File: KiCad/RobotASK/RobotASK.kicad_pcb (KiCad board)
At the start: 2 copper layers, 80 x 50 mm, 14 parts, among them J1 Conn_01x04_Pin, J2 Conn_01x04_Pin, J3 Conn_01x04_Pin, J4 Conn_01x04_Pin, J5 Conn_01x04_Pin, J6 Conn_01x04_Pin, J7 Conn_01x02_Pin, J8 Conn_01x03_Pin, SW2 SW_Omron_B3FS, U1 ATmega328-P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

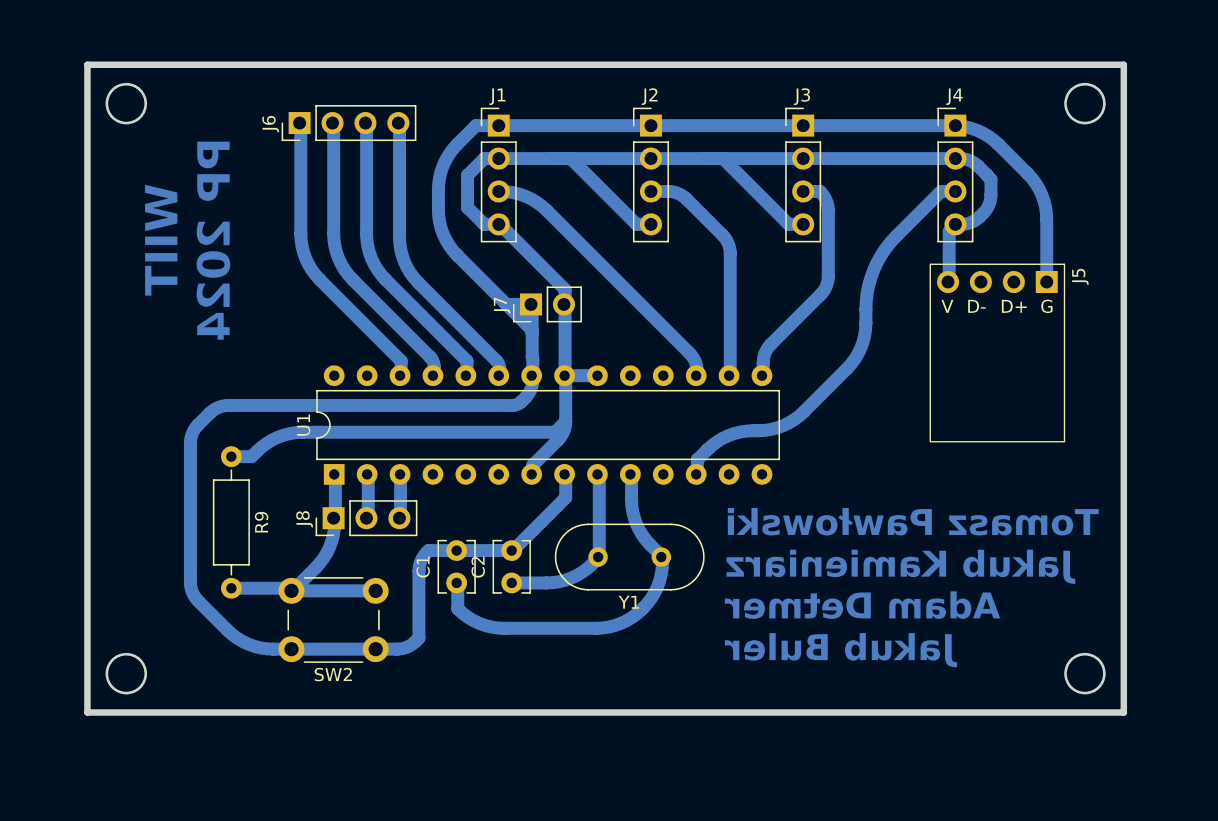
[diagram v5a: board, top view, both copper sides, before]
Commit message: Poprawki kodu, zwiększenie otworów na komponenty na 1mm, nowe wydruki do termotransferu i nawiercania otworów, poukładanie nieaktualnych wydruków UV
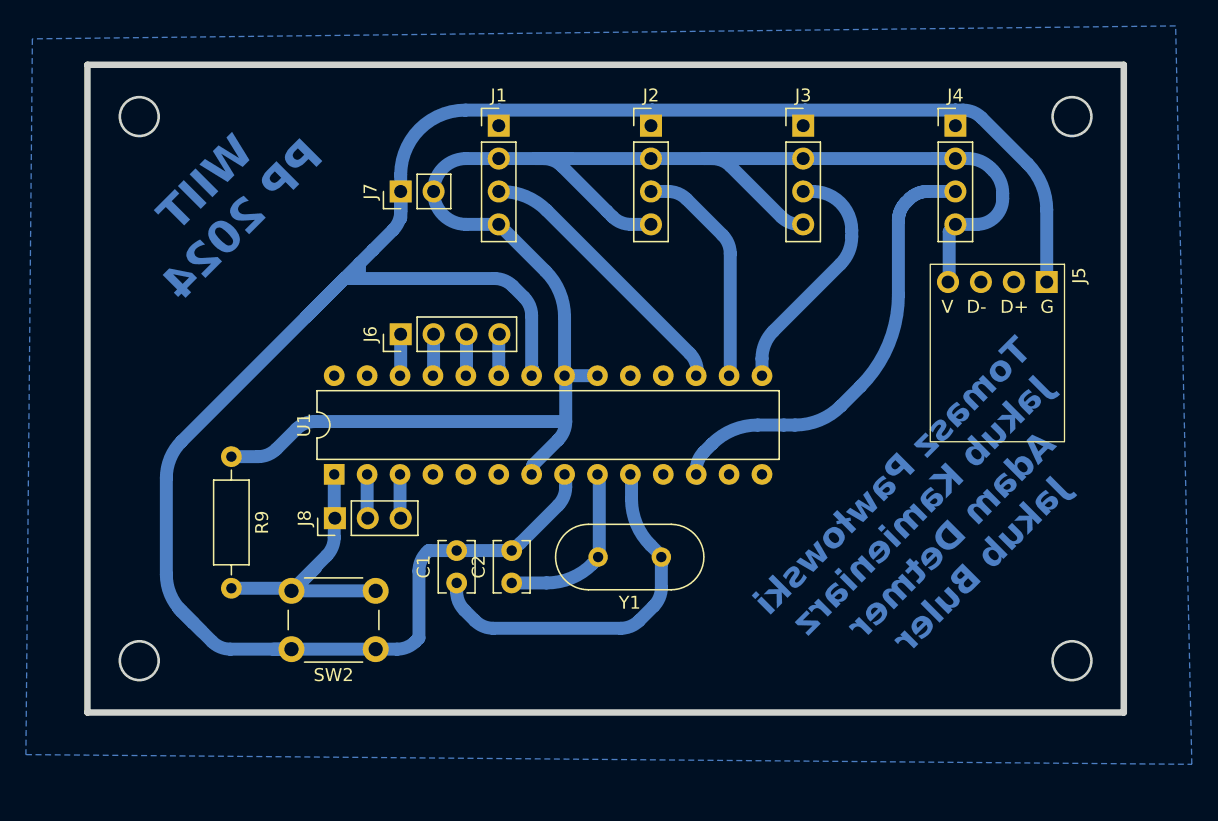
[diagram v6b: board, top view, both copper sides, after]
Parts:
- moved J6 18.1 mm to (94.2, 70.8)
- moved J7 13.3 mm to (94.2, 59.8)
- moved J8 0.10 mm to (89.1, 85.0)
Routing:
- net GND: track 162.3 -> 187.0 mm
- net PH3: track 22.5 -> 3.29 mm
- net PH1: track 22.5 -> 3.29 mm
- net PH2: track 22.5 -> 3.29 mm
- net PH0: track 22.5 -> 3.76 mm
- net +5V: track 128.0 -> 138.4 mm
- net ~RESET: track 21.3 -> 24.4 mm
- net SERV3: track 32.7 -> 35.5 mm
- net SERV2: track 17.5 -> 19.1 mm
- net CRY2: track 28.5 -> 29.4 mm
- added copper zone on B.Cu, net GND
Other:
- outline, holes or cut-outs redrawn

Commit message: renders
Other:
- board text added: "+5V"
- board text added: "10k"
- board text added: "16Mhz"
- board text added: "22pF"
- board text added: "ATmega328"
- board text added: "GND"
- board text added: "P0"
- board text added: "P1"
- board text added: "P2"
- board text added: "P3"
- board text added: "RESET"
- board text added: "RX"
- board text added: "S0"
- board text added: "S1"
- board text added: "S2"
- board text added: "S3"
- board text added: "TX"
